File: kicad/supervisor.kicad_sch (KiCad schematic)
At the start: 48 parts, among them J1 USB-C, J2 JTAG, J51 SUP_SWD, SW1 BOOTSEL, U7 RP2350B, U8 W25Q32JVZP, Y1 12MHz

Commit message: power input: single USB-C with CH224K PD sink at 9V, Schottky OR-ing, degraded 5V mode; record missing board-ID pins
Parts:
- removed R29: 33, Resistor_SMD:R_0402_1005Metric, symbol Device:R
- added C98: 1uF, Capacitor_SMD:C_0402_1005Metric, symbol Device:C
- added U18: CH224K, Package_DFN_QFN:QFN-12-1EP_3x3mm_P0.5mm_EP1.45x1.45mm, symbol Interface_USB:CH224K
- R10: value 5.1k -> 33
- R9: value 5.1k -> 10k
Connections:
- net +3V3: now also R9.1
- net CFG_CCLK: now also R17.2; no longer R18.2
- net CFG_DONE: now also R16.2; no longer R17.2
- net CFG_INIT_B: now also R15.2; no longer R16.2
- net CFG_PROG_B: now also R14.2; no longer R15.2
- net DBG_TCK: now also R23.2; no longer R24.2
- net DBG_TDI: now also R25.2; no longer R26.2
- net DBG_TDO: now also R26.2; no longer R27.2
- net DBG_TMS: now also R24.2; no longer R25.2
- net FLASH_CS_B: now also R18.2; no longer R19.2
- net FLASH_D0_MOSI: now also R19.2; no longer R20.2
- net FLASH_D1_MISO: now also R20.2; no longer R21.2
- net FLASH_D2_WP: now also R21.2; no longer R22.2
- net FLASH_D3_HOLD: now also R22.2; no longer R23.2
- net GND: now also C98.2, U18.11 (GND); no longer R10.2, R9.2
- net JTAG_TCK: now also R10.2; no longer R11.2
- net JTAG_TDI: now also R12.2; no longer R13.2
- net JTAG_TDO: now also R13.2; no longer R14.2
- net JTAG_TMS: now also R11.2; no longer R12.2
- net SB_UART_RX: now also R27.2; no longer R28.2
- net SB_UART_TX: now also R28.2
- net SUP_CCLK: now also R17.1; no longer R18.1
- net SUP_DBG_TCK: now also R23.1; no longer R24.1
- net SUP_DBG_TDI: now also R25.1; no longer R26.1
- net SUP_DBG_TDO: now also R26.1; no longer R27.1
- net SUP_DBG_TMS: now also R24.1; no longer R25.1
- net SUP_DONE: now also R16.1; no longer R17.1
- net SUP_FCS_B: now also R18.1; no longer R19.1
- net SUP_FD0: now also R19.1; no longer R20.1
- net SUP_FD1: now also R20.1; no longer R21.1
- net SUP_FD2: now also R21.1; no longer R22.1
- net SUP_FD3: now also R22.1; no longer R23.1
- net SUP_INIT_B: now also R15.1; no longer R16.1
- net SUP_JTAG_TCK: now also R10.1; no longer R11.1
- net SUP_JTAG_TDI: now also R12.1; no longer R13.1
- net SUP_JTAG_TDO: now also R13.1; no longer R14.1
- net SUP_JTAG_TMS: now also R11.1; no longer R12.1
- net SUP_PROG_B: now also R14.1; no longer R15.1
- net SUP_UART_RX: now also R28.1
- net SUP_UART_TX: now also R27.1; no longer R28.1
- net USB_CC1: now also U18.7 (CC1); no longer R9.1
- net USB_CC2: now also U18.6 (CC2); no longer R10.1
- net VBUS: now also U18.8 (VBUS)
- net BOARDID_0 renamed PD_CFG1
- net PD_CFG1: now also U18.9 (CFG1)
- net BOARDID_1 renamed PD_CFG2
- net PD_CFG2: now also U18.2 (CFG2)
- net BOARDID_2 renamed PD_CFG3
- net PD_CFG3: now also U18.3 (CFG3)
- net BOARDID_3 renamed PD_PG
- net PD_PG: now also R9.2, U18.10 (PG)
- net MON_12V renamed MON_VSYS
- new net PD_VDD: C98.1, U18.1 (VDD)
- no-connect marks 3 -> 5
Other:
- note added: "USB-PD sink"
- moved on the sheet: J1, J2, R10, R11, R12, R13, R14, R15, R16, R17, R18, R19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

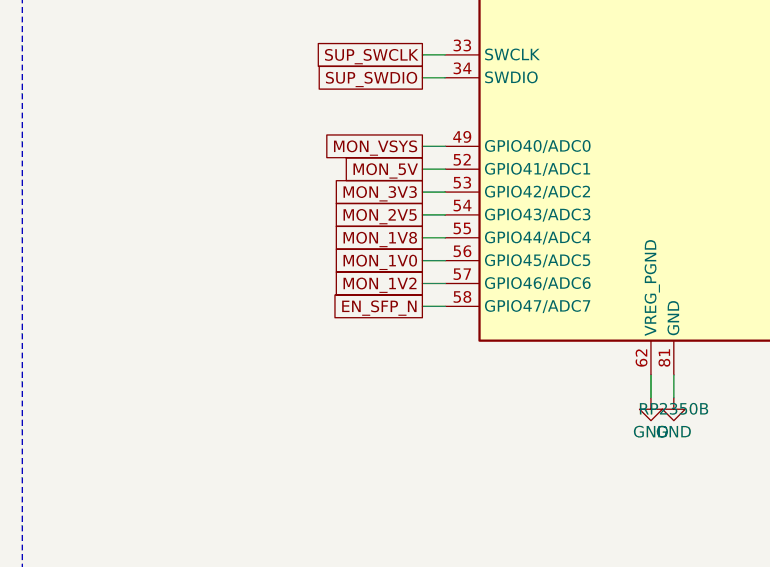
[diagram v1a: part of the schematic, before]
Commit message: assume 5V for function, PD only for headroom: boost 12V AUX from the 5V rail
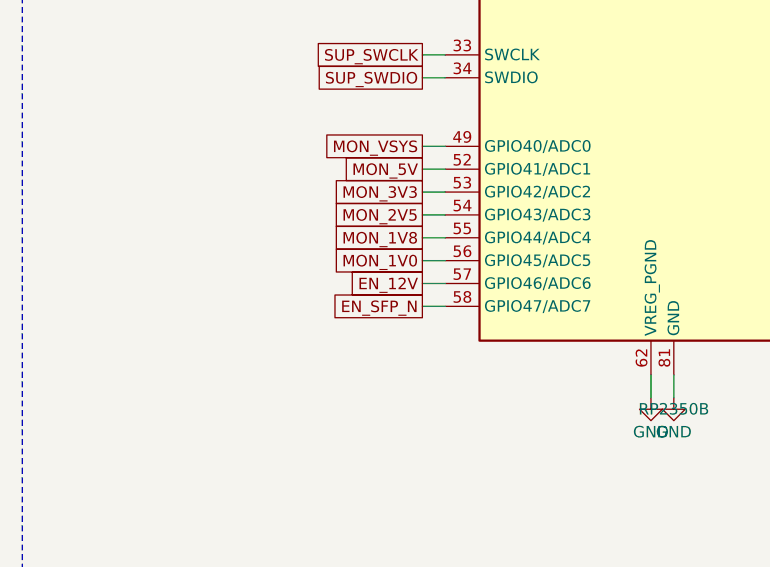
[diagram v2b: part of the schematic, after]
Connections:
- net MON_1V2 renamed EN_12V

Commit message: supervisor flash: document the role, add BOOTSEL series resistor
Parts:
- added R29: 33, Resistor_SMD:R_0402_1005Metric, symbol Device:R
- R10: value 33 -> 1k
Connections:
- net CFG_CCLK: now also R18.2; no longer R17.2
- net CFG_DONE: now also R17.2; no longer R16.2
- net CFG_INIT_B: now also R16.2; no longer R15.2
- net CFG_PROG_B: now also R15.2; no longer R14.2
- net DBG_TCK: now also R24.2; no longer R23.2
- net DBG_TDI: now also R26.2; no longer R25.2
- net DBG_TDO: now also R27.2; no longer R26.2
- net DBG_TMS: now also R25.2; no longer R24.2
- net FLASH_CS_B: now also R19.2; no longer R18.2
- net FLASH_D0_MOSI: now also R20.2; no longer R19.2
- net FLASH_D1_MISO: now also R21.2; no longer R20.2
- net FLASH_D2_WP: now also R22.2; no longer R21.2
- net FLASH_D3_HOLD: now also R23.2; no longer R22.2
- net JTAG_TCK: now also R11.2; no longer R10.2
- net JTAG_TDI: now also R13.2; no longer R12.2
- net JTAG_TDO: now also R14.2; no longer R13.2
- net JTAG_TMS: now also R12.2; no longer R11.2
- net SB_UART_RX: now also R28.2; no longer R27.2
- net SB_UART_TX: now also R29.2; no longer R28.2
- net SUPF_CS: now also R10.1; no longer SW1.1
- net SUP_CCLK: now also R18.1; no longer R17.1
- net SUP_DBG_TCK: now also R24.1; no longer R23.1
- net SUP_DBG_TDI: now also R26.1; no longer R25.1
- net SUP_DBG_TDO: now also R27.1; no longer R26.1
- net SUP_DBG_TMS: now also R25.1; no longer R24.1
- net SUP_DONE: now also R17.1; no longer R16.1
- net SUP_FCS_B: now also R19.1; no longer R18.1
- net SUP_FD0: now also R20.1; no longer R19.1
- net SUP_FD1: now also R21.1; no longer R20.1
- net SUP_FD2: now also R22.1; no longer R21.1
- net SUP_FD3: now also R23.1; no longer R22.1
- net SUP_INIT_B: now also R16.1; no longer R15.1
- net SUP_JTAG_TCK: now also R11.1; no longer R10.1
- net SUP_JTAG_TDI: now also R13.1; no longer R12.1
- net SUP_JTAG_TDO: now also R14.1; no longer R13.1
- net SUP_JTAG_TMS: now also R12.1; no longer R11.1
- net SUP_PROG_B: now also R15.1; no longer R14.1
- net SUP_UART_RX: now also R29.1; no longer R28.1
- net SUP_UART_TX: now also R28.1; no longer R27.1
- new net BOOTSEL_SW: R10.2, SW1.1
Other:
- note added: "BOOTSEL"
- moved on the sheet: J51, R10, R11, R12, R13, R14, R15, R16, R17, R18, R19, R20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

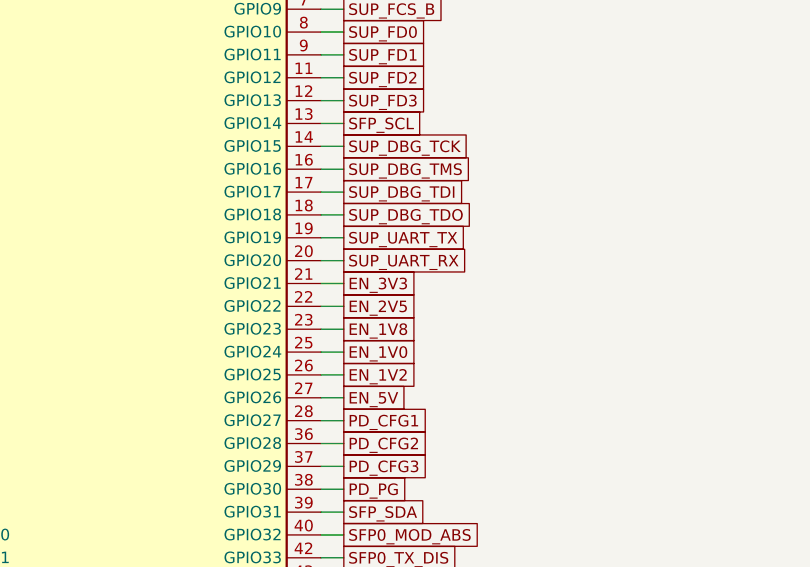
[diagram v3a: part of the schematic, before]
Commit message: fix boot deadlock (+3V3 now always-on off VSYS) and VBUS overvoltage hazard (switch, not diode)
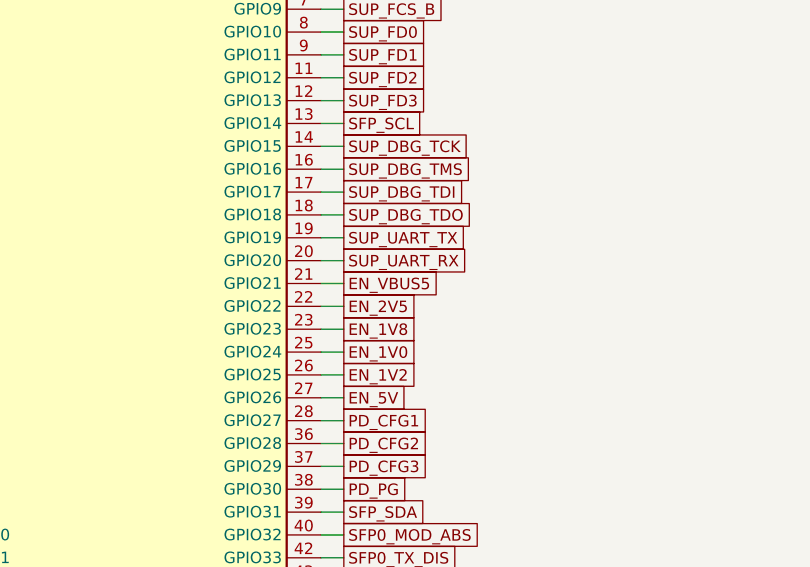
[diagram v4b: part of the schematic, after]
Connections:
- net EN_3V3 renamed EN_VBUS5

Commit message: audit response: fix 5V-overstressed translators, add USB ESD protection and keying posts, load the PCB, reconcile every stale doc
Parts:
- added D6: ESDA6V1BC6, Package_TO_SOT_SMD:SOT-666, symbol Power_Protection:ESDA6V1BC6
- added D7: SMBJ13A, Diode_SMD:D_SMB, symbol Device:D_TVS
- U7: footprint Package_DFN_QFN:QFN-80-1EP_10x10mm_P0.4mm_EP3.4x3.4mm_ThermalVias -> Package_DFN_QFN:QFN-80-1EP_10x10mm_P0.4mm_EP3.4x3.4mm
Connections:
- net GND: now also D6.2 (COM), D6.5 (COM), D7.2 (A2)
- net USB_CC1: now also D6.4 (TVS3)
- net USB_CC2: now also D6.6 (TVS4)
- net USB_DM: now also D6.3 (TVS2)
- net USB_DP: now also D6.1 (TVS1)
- net VBUS: now also D7.1 (A1)
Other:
- note added: "USB protection"
- moved on the sheet: C98, J51, R10, R9, SW1, U18

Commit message: fix 14 package mismatches, assert footprints against ki_fp_filters, rebalance fuses, correct JTAG and PD-voltage claims
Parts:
- D6: footprint Package_TO_SOT_SMD:SOT-666 -> Package_TO_SOT_SMD:SOT-23-6
- U18: footprint Package_DFN_QFN:QFN-12-1EP_3x3mm_P0.5mm_EP1.45x1.45mm -> Package_SO:SSOP-10-1EP_3.9x4.9mm_P1mm_EP2.1x3.3mm_ThermalVias
- U8: footprint Package_SON:Winbond_USON-8-1EP_3x2mm_P0.5mm_EP0.2x1.6mm -> Package_SON:WSON-8-1EP_6x5mm_P1.27mm_EP3.4x4mm
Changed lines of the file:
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@@
 		(property "Reference" "U8" (at 289.56 302.26 0) (effects (font (size 1.27 1.27))))
 		(property "Value" "W25Q32JVZP" (at 289.56 335.28 0) (effects (font (size 1.27 1.27))))
-		(property "Footprint" "Package_SON:Winbond_USON-8-1EP_3x2mm_P0.5mm_EP0.2x1.6mm" (at 289.56 335.28 0) (effects (font (size 1.27 1.27)) (hide yes)))
+		(property "Footprint" "Package_SON:WSON-8-1EP_6x5mm_P1.27mm_EP3.4x4mm" (at 289.56 335.28 0) (effects (font (size 1.27 1.27)) (hide yes)))
 		(property "LCSC" "C82317" (at 289.56 335.28 0) (effects (font (size 1.27 1.27)) (hide yes)))
 		(instances (project "odin" (path "/c44fb7fe-6133-ad34-68fd-fb66126197ef/3e2df089-f023-0194-2f85-195f6ca76ec6" (reference "U8") (unit 1))))
@@
 		(property "Reference" "D6" (at 82.55 444.5 0) (effects (font (size 1.27 1.27))))
 		(property "Value" "ESDA6V1BC6" (at 82.55 467.36 0) (effects (font (size 1.27 1.27))))
-		(property "Footprint" "Package_TO_SOT_SMD:SOT-666" (at 82.55 467.36 0) (effects (font (size 1.27 1.27)) (hide yes)))
+		(property "Footprint" "Package_TO_SOT_SMD:SOT-23-6" (at 82.55 467.36 0) (effects (font (size 1.27 1.27)) (hide yes)))
 		(instances (project "odin" (path "/c44fb7fe-6133-ad34-68fd-fb66126197ef/3e2df089-f023-0194-2f85-195f6ca76ec6" (reference "D6") (unit 1))))
 	)
@@
 		(property "Reference" "U18" (at 203.2 444.5 0) (effects (font (size 1.27 1.27))))
 		(property "Value" "CH224K" (at 203.2 472.44 0) (effects (font (size 1.27 1.27))))
-		(property "Footprint" "Package_DFN_QFN:QFN-12-1EP_3x3mm_P0.5mm_EP1.45x1.45mm" (at 203.2 472.44 0) (effects (font (size 1.27 1.27)) (hide yes)))
+		(property "Footprint" "Package_SO:SSOP-10-1EP_3.9x4.9mm_P1mm_EP2.1x3.3mm_ThermalVias" (at 203.2 472.44 0) (effects (font (size 1.27 1.27)) (hide yes)))
 		(instances (project "odin" (path "/c44fb7fe-6133-ad34-68fd-fb66126197ef/3e2df089-f023-0194-2f85-195f6ca76ec6" (reference "U18") (unit 1))))
 	)

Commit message: Update Odin hardware design, imported parts, and documentation
Include EasyEDA symbols, footprints and 3D models; revise FPGA allocation, power and extension buses; add qualification audits and user documentation.

Validation: EasyEDA audit, qualified parts, power budget and Python syntax pass. KiCad ERC reports 1 error and 319 warnings; DRC reports 90 violations, 499 unconnected items and 209 schematic parity issues. This is a work-in-progress design snapshot. Imported vendor assets retain their original formatting.
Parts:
- removed C80, C81, C82, C83, C84, C85, C86, C87, C88, C89, C90, C91, C96, C97: 100nF, Capacitor_SMD:C_0402_1005Metric, symbol Device:C
- removed C92: 4.7uF, Capacitor_SMD:C_0603_1608Metric, symbol Device:C
- removed C93: 10uF, Capacitor_SMD:C_0805_2012Metric, symbol Device:C
- removed C94, C95: 15pF, Capacitor_SMD:C_0402_1005Metric, symbol Device:C
- removed C98: 1uF, Capacitor_SMD:C_0402_1005Metric, symbol Device:C
- added C117, C118, C119, C120, C121, C122, C123, C124, C125, C126, C127, C128, C129, C130, C136, C137, C139: 100nF, Capacitor_SMD:C_0402_1005Metric, symbol Device:C
- added C131, C132, C133: 4.7uF, Capacitor_SMD:C_0603_1608Metric, symbol Device:C
- added C134, C135: 15pF, Capacitor_SMD:C_0402_1005Metric, symbol Device:C
- added C138: 1uF, Capacitor_SMD:C_0402_1005Metric, symbol Device:C
- added J52: PZ254V-11-02P, EasyEDA:HDR-TH_2P-P2.54-V-M, symbol EasyEDA:PZ254V-11-02P
- added R30, R31, R32: 33, Resistor_SMD:R_0402_1005Metric, symbol Device:R
- added R33: 0, Resistor_SMD:R_0402_1005Metric, symbol Device:R
- added R34: 10k, Resistor_SMD:R_0603_1608Metric, symbol Device:R
- added U20: SN74CB3Q3384APWR, EasyEDA:TSSOP-24_L7.8-W4.4-P0.65-LS6.4-BL, symbol 74xx:SN74CB3Q3384APW
- D6: footprint Package_TO_SOT_SMD:SOT-23-6 -> EasyEDA:SOT-23-6_L2.9-W1.6-P0.95-LS2.8-BR; LCSC (none) -> C495220
- D7: value SMBJ13A -> SMBJ13A-TR; footprint Diode_SMD:D_SMB -> EasyEDA:SMB_L4.6-W3.6-LS5.3-RD; symbol Device:D_TVS -> Device:D_Zener; LCSC (none) -> C133675
- J1: LCSC (none) -> C2894897
- J2: value JTAG -> FPGA JTAG; footprint Connector_PinHeader_2.54mm:PinHeader_2x05_P2.54mm_Vertical -> EasyEDA:IDC-TH_10P-P2.54_C5665; symbol Connector_Generic:Conn_02x05_Odd_Even -> EasyEDA:HDR-IDC-2.54-2X5P; LCSC (none) -> C5665
- J51: value SUP_SWD -> CTRL SWD; footprint Connector_PinHeader_2.54mm:PinHeader_1x03_P2.54mm_Vertical -> EasyEDA:CONN-SMD-3P-P1.00_BM03B-SRSS-TB-LF-SN; symbol Connector_Generic:Conn_01x03 -> EasyEDA:BM03B-SRSS-TB; LCSC (none) -> C160389
- L1: value 3.3uH -> 3.3uH AOTA-B201610S3R3-101-T; footprint Inductor_SMD:L_Bourns-SRN4018 -> EasyEDA:IND-SMD_L2.0-W1.6_AOTA-B201610S3R3-101-T; LCSC (none) -> C42411119
- R10: LCSC (none) -> C11702
- R11: value 33 -> 10k
- R12: value 33 -> 1k; LCSC (none) -> C11702
- R13: value 33 -> 10k; now not fitted
- R14, R15, R16, R17, R18, R19, R20, R21, R22, R23, R24, R25, R26, R27, R28, R29: LCSC (none) -> C25105
- R8: value 1k -> 33; LCSC (none) -> C25105
- R9: value 10k -> 1k; LCSC (none) -> C11702
- SW1: value BOOTSEL -> CTRL BOOT; footprint Button_Switch_SMD:SW_SPST_B3U-1000P -> EasyEDA:KEY-SMD_B3U-1000PM; LCSC (none) -> C231329
- U18: footprint Package_SO:SSOP-10-1EP_3.9x4.9mm_P1mm_EP2.1x3.3mm_ThermalVias -> EasyEDA:ESSOP-10_L4.9-W3.9-P1.0-LS6.0-TL-EP; LCSC (none) -> C970725
- U7: footprint Package_DFN_QFN:QFN-80-1EP_10x10mm_P0.4mm_EP3.4x3.4mm -> EasyEDA:QFN-80_L10.0-W10.0-P0.40-TL-EP3.4; LCSC (none) -> C42415655
- U8: footprint Package_SON:WSON-8-1EP_6x5mm_P1.27mm_EP3.4x4mm -> EasyEDA:WSON-8_L6.0-W5.0-P1.27-BL-EP; LCSC C82317 -> C571260
- Y1: value 12MHz -> 12MHz ABM8-272-T3; footprint Crystal:Crystal_SMD_3225-4Pin_3.2x2.5mm -> EasyEDA:CRYSTAL-SMD_4P-L3.2-W2.5-BL; LCSC (none) -> C20625731
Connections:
- net +1V1: now also C128.1, C129.1, C130.1, C132.1
- net +3V3: now also R10.1, R11.1, R13.1, C117.1, C118.1, C119.1, C120.1, C121.1, C122.1, C123.1, C124.1, C125.1, C126.1, C127.1, C131.1, C137.1, C139.1, J52.1, U20.13 (~{2OE}), U20.24 (VCC); no longer R9.1, U7.61 (VREG_AVDD)
- net BOOTSEL_SW: now also R12.2; no longer R10.2
- net CFG_CCLK: now also R21.2; no longer R18.2
- net CFG_DONE: now also R20.2; no longer R17.2
- net CFG_INIT_B: now also R19.2; no longer R16.2
- net CFG_PROG_B: now also R18.2; no longer R15.2
- net DBG_TCK: now also R27.2; no longer R24.2
- net DBG_TDI: now also R29.2; no longer R26.2
- net DBG_TDO: now also R30.2; no longer R27.2
- net DBG_TMS: now also R28.2; no longer R25.2
- net FLASH_CS_B: now also R22.2; no longer R19.2
- net FLASH_D0_MOSI: now also R23.2; no longer R20.2
- net FLASH_D1_MISO: now also R24.2; no longer R21.2
- net FLASH_D2_WP: now also R25.2; no longer R22.2
- net FLASH_D3_HOLD: now also R26.2; no longer R23.2
- net GND: now also C117.2, C118.2, C119.2, C120.2, C121.2, C122.2, C123.2, C124.2, C125.2, C126.2, C127.2, C128.2, C129.2, C130.2, C131.2, C132.2, C133.2, C134.2, C135.2, C136.2, C137.2, C138.2, C139.2, R34.2, U20.12 (GND)
- net JTAG_TCK: now also U20.2 (1B1); no longer R11.2
- net JTAG_TDI: now also U20.6 (1B3); no longer R13.2
- net JTAG_TDO: now also R33.2; no longer R14.2
- net JTAG_TMS: now also U20.5 (1B2); no longer R12.2
- net PD_PG: now also R11.2; no longer R9.2
- net PD_VDD: now also C138.1
- net SB_UART_RX: now also R31.2; no longer R28.2
- net SB_UART_TX: now also R32.2; no longer R29.2
- net SUPF_CS: now also R12.1, R13.2; no longer R10.1
- net SUP_CCLK: now also R21.1; no longer R18.1
- net SUP_DBG_TCK: now also R27.1; no longer R24.1
- net SUP_DBG_TDI: now also R29.1; no longer R26.1
- net SUP_DBG_TDO: now also R30.1; no longer R27.1
- net SUP_DBG_TMS: now also R28.1; no longer R25.1
- net SUP_DONE: now also R20.1; no longer R17.1
- net SUP_FCS_B: now also R22.1; no longer R19.1
- net SUP_FD0: now also R23.1; no longer R20.1
- net SUP_FD1: now also R24.1; no longer R21.1
- net SUP_FD2: now also R25.1; no longer R22.1
- net SUP_FD3: now also R26.1; no longer R23.1
- net SUP_INIT_B: now also R19.1; no longer R16.1
- net SUP_JTAG_TCK: now also R14.1; no longer R11.1
- net SUP_JTAG_TDI: now also R16.1; no longer R13.1
- net SUP_JTAG_TDO: now also R17.1; no longer R14.1
- net SUP_JTAG_TMS: now also R15.1; no longer R12.1
- net SUP_PROG_B: now also R18.1; no longer R15.1
- net SUP_RUN: now also R10.2, C136.1; no longer R8.2
- net SUP_UART_RX: now also R32.1; no longer R29.1
- net SUP_UART_TX: now also R31.1; no longer R28.1
- net SUP_XIN: now also C134.1
- net SUP_XOUT: now also R9.1; no longer Y1.3
- net EXT_EN: now reaches U7.6 (GPIO8)
- net EN_SFP_N renamed EXT_FAULT
- new net EXTERNAL_JTAG_SELECTED: J52.2, R34.1, U20.1 (~{1OE})
- new net JTAG_TDO_SW: R33.1, U20.9 (1B4)
- new net SUP_VREG_AVDD: C133.1, R8.2, U7.61 (VREG_AVDD)
- new net SUP_XTAL_OUT: C135.1, R9.2, Y1.3
- new net SWJ_TCK: R14.2, U20.3 (1A1)
- new net SWJ_TDI: R16.2, U20.7 (1A3)
- new net SWJ_TDO: R17.2, U20.8 (1A4)
- new net SWJ_TMS: R15.2, U20.4 (1A2)
- no-connect marks 5 -> 18
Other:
- note added: "JTAG owner selection"
- note added: "RUN"
- note added: "SUPERVISOR — Board controller: RP2350B, USB-C, startup memory and FPGA control — HW 0.1.0-proto.1"
- note added: "U7 board controller"
- note added: "U7 core regulator (RP-008280 s2.1)"
- note added: "board controller SWD"
- note added: "board controller startup memory"
- note added: "crystal (RP-008280 s4)"
- note removed: "SUPERVISOR — RP2350B supervisor, USB-C, flash, and the links to the FPGA"
- note removed: "U7 supervisor"
- note removed: "crystal"
- note removed: "supervisor SWD"
- note removed: "supervisor boot flash"
- moved on the sheet: D6, D7, J1, J2, L1, R10, R11, R12, R14, R15, R16, R17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

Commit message: wip
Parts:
- removed C139: 100nF, Capacitor_SMD:C_0402_1005Metric, symbol Device:C
- added C116: 100nF, Capacitor_SMD:C_0402_1005Metric, symbol Device:C
- C130: value 100nF -> 4.7uF; footprint Capacitor_SMD:C_0402_1005Metric -> Capacitor_SMD:C_0603_1608Metric; LCSC C1525 -> C277476
- C133: value 4.7uF -> 15pF; footprint Capacitor_SMD:C_0603_1608Metric -> Capacitor_SMD:C_0402_1005Metric; LCSC C277476 -> (none)
- C135: value 15pF -> 100nF; LCSC (none) -> C1525
- C137: value 100nF -> 1uF; LCSC C1525 -> (none)
- C138: value 1uF -> 100nF; LCSC (none) -> C1525
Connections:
- net +1V1: now also C127.1, C131.1; no longer C130.1, C132.1
- net +3V3: now also C130.1, C136.1, C138.1, C116.1; no longer C127.1, C131.1, C137.1
- net GND: now also C116.2
- net PD_VDD: now also C137.1; no longer C138.1
- net SUP_RUN: now also C135.1; no longer C136.1
- net SUP_VREG_AVDD: now also C132.1; no longer C133.1
- net SUP_XIN: now also C133.1; no longer C134.1
- net SUP_XTAL_OUT: now also C134.1; no longer C135.1
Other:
- moved on the sheet: C117, C118, C119, C120, C121, C122, C123, C124, C125, C126, C127, C128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
